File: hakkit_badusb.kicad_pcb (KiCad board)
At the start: 2 copper layers, 16.4 x 42.8 mm, 20 parts, among them J1 USB3_A, U1 RP2040, U2 W25Q128JVP, U3 LT1962-3.3, Y1 12MHz Cryst

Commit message: remade pcb
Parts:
- added J2: Micro_SD_Card, Connector_Card:microSD_HC_Molex_47219-2001, B.Cu at (112.4, 45.8)
- C1, C2, C3, C4, J1, R1, R3, R4, R5, U3: moved to B.Cu
- moved J1 53.5 mm to (146.9, 45.8), turned to 0 degrees
- moved R1 38.4 mm to (133.8, 52.0), turned to 180 degrees
- moved Y1 37.0 mm to (130.5, 45.4)
- moved R5 35.9 mm to (133.8, 41.4)
- moved C3 34.7 mm to (130.0, 44.2)
- moved C5 34.2 mm to (130.7, 41.0)
- moved C2 33.0 mm to (127.7, 52.0), turned to 180 degrees
- moved C4 32.0 mm to (130.8, 52.0), turned to 180 degrees
- moved U1 31.5 mm to (122.8, 45.2), turned to 45 degrees
- moved C6 30.8 mm to (130.7, 49.5)
- moved R7 30.6 mm to (118.9, 50.1), turned to -135 degrees
- moved U3 29.9 mm to (130.4, 49.0), turned to 0 degrees
- moved C1 27.5 mm to (131.3, 40.0), turned to 180 degrees
- moved R6 27.4 mm to (117.0, 48.0), turned to -135 degrees
- moved D1 25.9 mm to (112.1, 51.6), turned to 180 degrees
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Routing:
- net GND: track 46.4 -> 68.8 mm, vias 6 -> 0
- net /SD_MISO: track 0.00 -> 21.3 mm, vias 0 -> 1
- net Net-(U1-XIN): track 30.2 -> 9.06 mm, vias 3 -> 0
- net /SD_SCK: track 0.00 -> 17.0 mm, vias 0 -> 1
- net +3V3: track 0.00 -> 16.9 mm, vias 0 -> 2
- net +5V: track 26.4 -> 9.92 mm, vias 3 -> 0
- net /SD_MOSI: track 0.00 -> 16.0 mm, vias 0 -> 1
- net Net-(U1-QSPI_SD1): track 0.00 -> 10.6 mm
- net Net-(U1-QSPI_SD2): track 0.00 -> 9.35 mm
- net Net-(J1-DRAIN): track 35.5 -> 26.2 mm
- net Net-(D1-RA): track 15.0 -> 7.27 mm, vias 2 -> 0
- net Net-(U1-RUN): track 7.41 -> 0.00 mm
- net Net-(U1-XOUT): track 4.31 -> 10.7 mm
- net Net-(U1-~{QSPI_SS}): track 19.5 -> 13.1 mm, vias 3 -> 0
- net Net-(U1-QSPI_SD3): track 0.00 -> 5.39 mm
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- added copper zone on B.Cu, net +3V3
- added copper zone on F.Cu, net GND
- removed copper zone on F.Cu, net +3V3
- removed copper zone on B.Cu, net GND
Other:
- board size 16.4 x 42.8 mm -> 36.5 x 18 mm

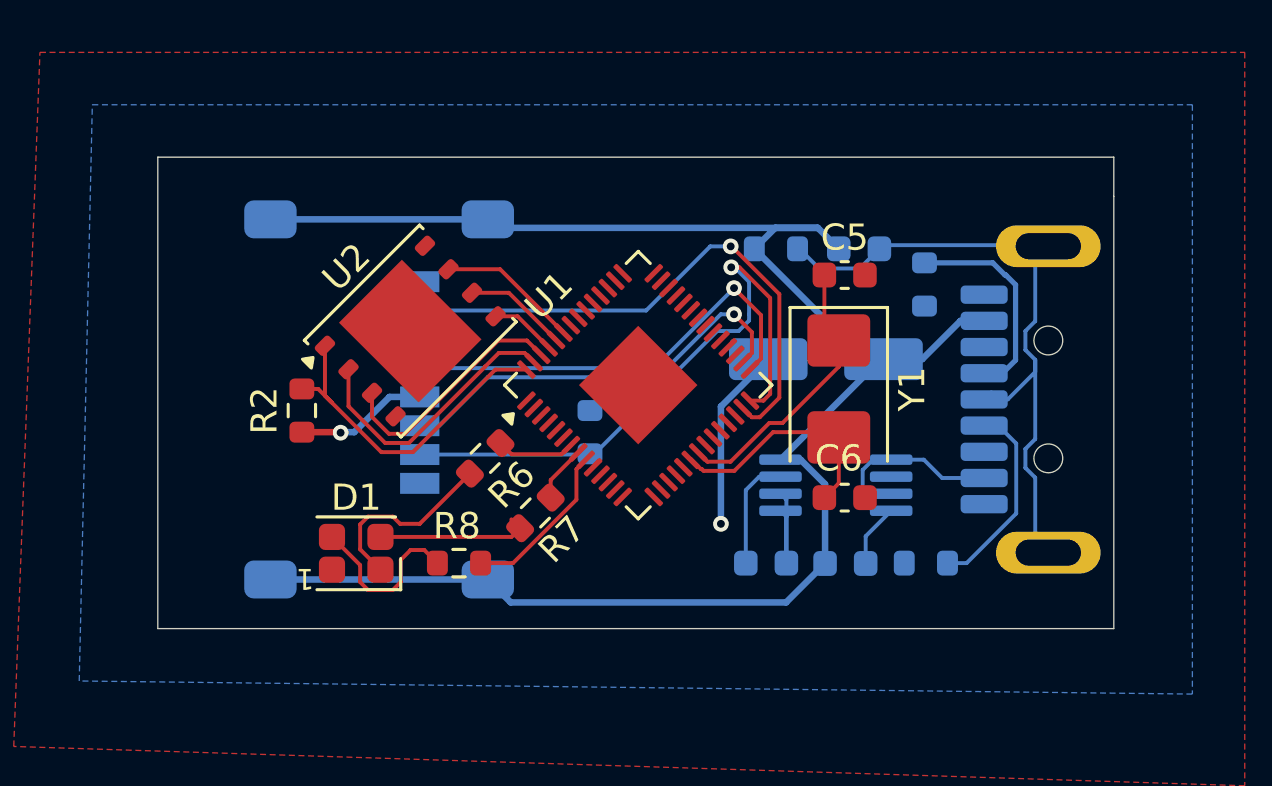
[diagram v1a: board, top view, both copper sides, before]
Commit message: finished board | must redo cause of components unaiavalbility
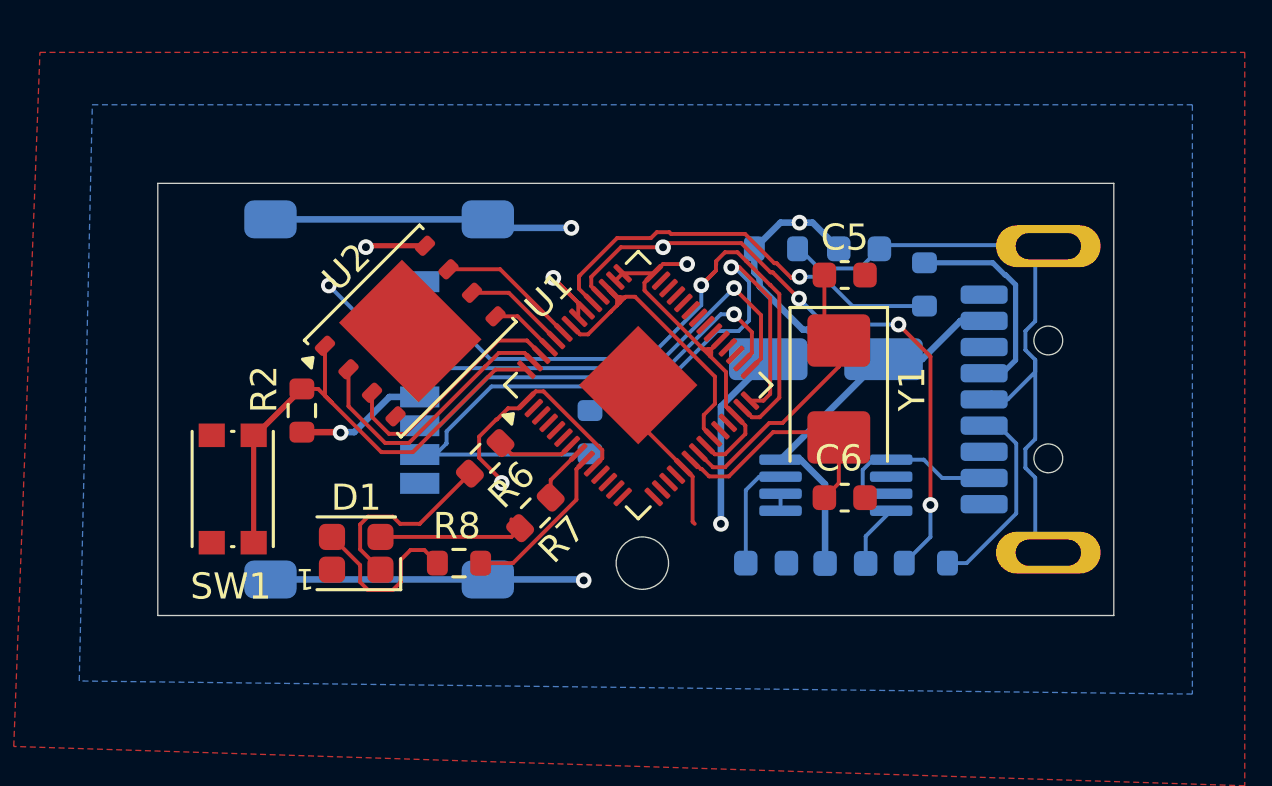
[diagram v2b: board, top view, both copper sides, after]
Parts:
- added SW1: SW_Push, Button_Switch_SMD:SW_Push_1P1T_NO_CK_KMR2, F.Cu at (107.4, 49.2)
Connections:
- U1 pad 1: Net-(U1-RUN) -> +3V3
- U1 pad 10: Net-(U1-RUN) -> +3V3
- U1 pad 22: Net-(U1-RUN) -> +3V3
- U1 pad 26: Net-(U1-RUN) -> +3V3
- U1 pad 33: Net-(U1-RUN) -> +3V3
- U1 pad 42: Net-(U1-RUN) -> +3V3
- U1 pad 49: Net-(U1-RUN) -> +3V3
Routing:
- net +3V3: track 16.9 -> 42.6 mm, vias 2 -> 6
- net Net-(U1-USB_DM): track 0.00 -> 24.4 mm, vias 0 -> 4
- net Net-(U1-USB_DP): track 0.00 -> 16.8 mm, vias 0 -> 1
- net Net-(U1-VREG_VOUT): track 0.00 -> 12.5 mm
- net Net-(U1-~{QSPI_SS}): track 13.1 -> 22.6 mm
- net GND: track 68.8 -> 60.8 mm, vias 0 -> 4
- net /SD_CS: track 23.6 -> 30.5 mm
- net /SD_MISO: track 21.3 -> 24.1 mm
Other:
- board size 36.5 x 18 mm -> 36.5 x 16.5 mm

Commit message: final pcb must order
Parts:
- removed D1: LED_KRGB, LED_SMD:LED_RGB_Lumex_SML-LXT0805SIUGUBW
- removed J1: USB3_A, Connector_USB:USB3_A_Plug_Wuerth_692112030100_Horizontal
- removed R6, R7, R8: 220R, Resistor_SMD:R_0603_1608Metric
- removed U2: W25Q128JVP, Package_SON:WSON-8-1EP_6x5mm_P1.27mm_EP3.4x4.3mm
- removed Y1: 12MHz Cryst, Crystal:Crystal_SMD_5032-2Pin_5.0x3.2mm
- added D2: WS2812B, LED_SMD:LED_WS2812B_PLCC4_5.0x5.0mm_P3.2mm, F.Cu at (115.1, 49.6)
- added J3: USB_A, Connector_USB:USB_A_Connfly_DS1098_Horizontal, B.Cu at (146.3, 46.0)
- added U4: W25Q16JVSS, Package_SO:SOIC-8_5.3x5.3mm_P1.27mm, F.Cu at (112.6, 42.4)
- added Y2: Crystal 12MHz, Crystal:Crystal_SMD_3225-4Pin_3.2x2.5mm, F.Cu at (130.7, 44.9)
- moved R2 1.83 mm to (110.0, 48.0)
- moved R5 1.36 mm to (133.8, 40.0)
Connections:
- U1 pad 7: Net-(U1-GPIO5) -> unconnected-(U1-GPIO5-Pad7)
- U1 pad 8: Net-(U1-GPIO6) -> unconnected-(U1-GPIO6-Pad8)
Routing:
- net Net-(U1-QSPI_SD1): track 10.6 -> 18.1 mm
- net Net-(D1-RA): track 7.27 -> 0.00 mm
- net Net-(U1-QSPI_SD2): track 9.35 -> 16.4 mm
- net Net-(D1-BA): track 6.69 -> 0.00 mm
- net Net-(U1-XIN): track 9.24 -> 15.6 mm
- net Net-(D1-GA): track 6.31 -> 0.00 mm
- net /USB_D-: track 7.59 -> 12.4 mm
- net GND: track 60.8 -> 63.9 mm
- net Net-(U1-GPIO5): track 3.01 -> 0.00 mm
- net Net-(D2-DIN): track 6.33 -> 3.66 mm
- net /USB_D+: track 8.11 -> 10.7 mm
- net Net-(J3-Shield): track 26.2 -> 23.8 mm
- net Net-(U1-~{QSPI_SS}): track 22.6 -> 24.7 mm
- net Net-(U1-GPIO6): track 2.16 -> 0.00 mm
- net Net-(U1-QSPI_SD3): track 5.39 -> 3.95 mm
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
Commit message: must redo tf-01a
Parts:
- removed J2: Micro_SD_Card, Connector_Card:microSD_HC_Molex_47219-2001
- removed R4: 10kR, Resistor_SMD:R_0603_1608Metric
- added MICRO_SD1: TF-01A, TF-01A:TF-01A, B.Cu at (108.5, 46.0)
- added R6: 10kR, Resistor_SMD:R_0603_1608Metric, B.Cu at (119.3, 45.0)
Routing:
- net /SD_CS: track 30.5 -> 19.5 mm
- net +3V3: track 42.9 -> 33.7 mm
- net GND: track 63.9 -> 60.8 mm, vias 4 -> 3
- net /SD_MOSI: track 16.0 -> 16.8 mm
- net Net-(D2-DIN): track 3.66 -> 4.39 mm
- net Net-(U1-USB_DP): track 17.4 -> 17.9 mm
- net /SD_MISO: track 24.1 -> 24.0 mm, vias 1 -> 3
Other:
- board size 36.5 x 16.5 mm -> 40.7 x 18.8 mm
